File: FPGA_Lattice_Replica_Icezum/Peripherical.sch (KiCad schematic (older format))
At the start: 33 parts, among them J15 1x4_male_pin_Header_2.54mm, J16 1x4_male_pin_Header_2.54mm, J17 1x4_male_pin_Header_2.54mm, SW1 SW1, SW2 Switch_4p, U7 ADS7924

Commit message: se corrigieron errores de huellas y referencias que genereban errores cuando se hacia el diseño PCB
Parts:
- LD0, LD1, LD2, LD3, LD4, LD5, LD6, LD7: symbol Device:LED -> icezum:LED
- R17, R18: footprint footprints:R_Array_Convex_4x0603 -> footprints:R_0402
- SW1, SW2: symbol icezum:Switch_4p -> icezum:Switch
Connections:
- net +3V3: now also SW1.2, SW2.2; no longer SW1.3, SW1.4, SW2.3, SW2.4
- net GND: now also LD0.K, LD1.K, LD2.K, LD3.K, LD4.K, LD5.K, LD6.K, LD7.K; no longer LD0.1 (K), LD1.1 (K), LD2.1 (K), LD3.1 (K), LD4.1 (K), LD5.1 (K), LD6.1 (K), LD7.1 (K)
- net U_SW1: no longer SW1.2
- net U_SW2: no longer SW2.2
- net at R17.1: now also LD0.A; no longer LD0.2 (A)
- net at R18.1: now also LD1.A; no longer LD1.2 (A)
- net at R40.1: now also LD2.A; no longer LD2.2 (A)
- net at R41.1: now also LD3.A; no longer LD3.2 (A)
- net at R42.1: now also LD4.A; no longer LD4.2 (A)
- net at R43.1: now also LD5.A; no longer LD5.2 (A)
- net at R44.1: now also LD6.A; no longer LD6.2 (A)
- net at R45.1: now also LD7.A; no longer LD7.2 (A)
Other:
- moved on the sheet: SW1, SW2
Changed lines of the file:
@@
 $EndDescr
 $Comp
-L Device:LED LD0
+L icezum:LED LD0
 U 1 1 5D1D395A
-P 9200 1500
-F 0 "LD0" H 9193 1245 50  0000 C CNN
-F 1 "Green" H 9193 1336 50  0000 C CNN
-F 2 "footprints:LED_0603" H 9200 1500 50  0001 C CNN
-F 3 "~" H 9200 1500 50  0001 C CNN
-	1    9200 1500
-	-1   0    0    1
-$EndComp
-$Comp
-L Device:LED LD1
+P 8950 1500
+F 0 "LD0" H 9200 1300 50  0000 C CNN
+F 1 "Green" H 9050 1400 50  0000 C CNN
+F 2 "footprints:LED_0603" H 8950 1500 50  0001 C CNN
+F 3 "~" H 8950 1500 50  0001 C CNN
+	1    8950 1500
+	1    0    0    -1
+$EndComp
+$Comp
+L icezum:LED LD1
 U 1 1 5D1D4304
-P 9200 2000
-F 0 "LD1" H 9193 1745 50  0000 C CNN
-F 1 "Green" H 9193 1836 50  0000 C CNN
-F 2 "footprints:LED_0603" H 9200 2000 50  0001 C CNN
-F 3 "~" H 9200 2000 50  0001 C CNN
-	1    9200 2000
-	-1   0    0    1
-$EndComp
-$Comp
-L Device:LED LD2
+P 8950 2000
+F 0 "LD1" H 9200 1800 50  0000 C CNN
+F 1 "Green" H 9050 1900 50  0000 C CNN
+F 2 "footprints:LED_0603" H 8950 2000 50  0001 C CNN
+F 3 "~" H 8950 2000 50  0001 C CNN
+	1    8950 2000
+	1    0    0    -1
+$EndComp
+$Comp
+L icezum:LED LD2
 U 1 1 5D1D467C
-P 9200 2550
-F 0 "LD2" H 9193 2295 50  0000 C CNN
-F 1 "Green" H 9193 2386 50  0000 C CNN
-F 2 "footprints:LED_0603" H 9200 2550 50  0001 C CNN
-F 3 "~" H 9200 2550 50  0001 C CNN
-	1    9200 2550
-	-1   0    0    1
-$EndComp
-$Comp
-L Device:LED LD3
+P 8950 2550
+F 0 "LD2" H 9200 2350 50  0000 C CNN
+F 1 "Green" H 9050 2450 50  0000 C CNN
+F 2 "footprints:LED_0603" H 8950 2550 50  0001 C CNN
+F 3 "~" H 8950 2550 50  0001 C CNN
+	1    8950 2550
+	1    0    0    -1
+$EndComp
+$Comp
+L icezum:LED LD3
 U 1 1 5D1D4941
-P 9200 3100
-F 0 "LD3" H 9193 2845 50  0000 C CNN
-F 1 "Green" H 9193 2936 50  0000 C CNN
-F 2 "footprints:LED_0603" H 9200 3100 50  0001 C CNN
-F 3 "~" H 9200 3100 50  0001 C CNN
-	1    9200 3100
-	-1   0    0    1
-$EndComp
-$Comp
-L Device:LED LD4
+P 8950 3100
+F 0 "LD3" H 9200 2900 50  0000 C CNN
+F 1 "Green" H 9050 3000 50  0000 C CNN
+F 2 "footprints:LED_0603" H 8950 3100 50  0001 C CNN
+F 3 "~" H 8950 3100 50  0001 C CNN
+	1    8950 3100
+	1    0    0    -1
+$EndComp
+$Comp
+L icezum:LED LD4
 U 1 1 5D1D4BE4
-P 9200 3700
-F 0 "LD4" H 9193 3445 50  0000 C CNN
-F 1 "Green" H 9193 3536 50  0000 C CNN
-F 2 "footprints:LED_0603" H 9200 3700 50  0001 C CNN
-F 3 "~" H 9200 3700 50  0001 C CNN
-	1    9200 3700
-	-1   0    0    1
-$EndComp
-$Comp
-L Device:LED LD5
+P 8950 3700
+F 0 "LD4" H 9200 3500 50  0000 C CNN
+F 1 "Green" H 9050 3600 50  0000 C CNN
+F 2 "footprints:LED_0603" H 8950 3700 50  0001 C CNN
+F 3 "~" H 8950 3700 50  0001 C CNN
+	1    8950 3700
+	1    0    0    -1
+$EndComp
+$Comp
+L icezum:LED LD5
 U 1 1 5D1D4EB3
-P 9200 4300
-F 0 "LD5" H 9193 4045 50  0000 C CNN
-F 1 "Green" H 9193 4136 50  0000 C CNN
-F 2 "footprints:LED_0603" H 9200 4300 50  0001 C CNN
-F 3 "~" H 9200 4300 50  0001 C CNN
-	1    9200 4300
-	-1   0    0    1
-$EndComp
-$Comp
-L Device:LED LD6
+P 8950 4300
+F 0 "LD5" H 9200 4100 50  0000 C CNN
+F 1 "Green" H 9050 4200 50  0000 C CNN
+F 2 "footprints:LED_0603" H 8950 4300 50  0001 C CNN
+F 3 "~" H 8950 4300 50  0001 C CNN
+	1    8950 4300
+	1    0    0    -1
+$EndComp
+$Comp
+L icezum:LED LD6
 U 1 1 5D1D527D
-P 9200 4850
-F 0 "LD6" H 9193 4595 50  0000 C CNN
-F 1 "Green" H 9193 4686 50  0000 C CNN
-F 2 "footprints:LED_0603" H 9200 4850 50  0001 C CNN
-F 3 "~" H 9200 4850 50  0001 C CNN
-	1    9200 4850
-	-1   0    0    1
-$EndComp
-$Comp
-L Device:LED LD7
+P 8950 4850
+F 0 "LD6" H 9200 4650 50  0000 C CNN
+F 1 "Green" H 9050 4750 50  0000 C CNN
+F 2 "footprints:LED_0603" H 8950 4850 50  0001 C CNN
+F 3 "~" H 8950 4850 50  0001 C CNN
+	1    8950 4850
+	1    0    0    -1
+$EndComp
+$Comp
+L icezum:LED LD7
 U 1 1 5D1D55BB
-P 9200 5400
-F 0 "LD7" H 9193 5145 50  0000 C CNN
-F 1 "Green" H 9193 5236 50  0000 C CNN
-F 2 "footprints:LED_0603" H 9200 5400 50  0001 C CNN
-F 3 "~" H 9200 5400 50  0001 C CNN
-	1    9200 5400
-	-1   0    0    1
+P 8950 5400
+F 0 "LD7" H 9200 5200 50  0000 C CNN
+F 1 "Green" H 9050 5300 50  0000 C CNN
+F 2 "footprints:LED_0603" H 8950 5400 50  0001 C CNN
+F 3 "~" H 8950 5400 50  0001 C CNN
+	1    8950 5400
+	1    0    0    -1
 $EndComp
 $Comp
@@
 F 0 "R17" V 8393 1500 50  0000 C CNN
 F 1 "2K2±5% 0.063W" V 8484 1500 50  0000 C CNN
-F 2 "footprints:R_Array_Convex_4x0603" V 8530 1500 50  0001 C CNN
+F 2 "footprints:R_0402" V 8530 1500 50  0001 C CNN
 F 3 "~" H 8600 1500 50  0001 C CNN
 	1    8600 1500
@@
 F 0 "R18" V 8393 2000 50  0000 C CNN
 F 1 "2K2±5% 0.063W" V 8484 2000 50  0000 C CNN
-F 2 "footprints:R_Array_Convex_4x0603" V 8530 2000 50  0001 C CNN
+F 2 "footprints:R_0402" V 8530 2000 50  0001 C CNN
 F 3 "~" H 8600 2000 50  0001 C CNN
 	1    8600 2000
@@
 	1    0    0    -1
 $EndComp
-Wire Wire Line
-	9350 1500 9650 1500
-Wire Wire Line
-	9650 1500 9650 2000
-Wire Wire Line
-	9350 5400 9650 5400
-Connection ~ 9650 5400
-Wire Wire Line
-	9650 5400 9650 5700
-Wire Wire Line
-	9350 4850 9650 4850
-Connection ~ 9650 4850
-Wire Wire Line
-	9650 4850 9650 5400
-Wire Wire Line
-	9350 4300 9650 4300
-Connection ~ 9650 4300
-Wire Wire Line
-	9650 4300 9650 4850
-Wire Wire Line
-	9350 3700 9650 3700
-Connection ~ 9650 3700
-Wire Wire Line
-	9650 3700 9650 4300
-Wire Wire Line
-	9350 3100 9650 3100
-Connection ~ 9650 3100
-Wire Wire Line
-	9650 3100 9650 3700
-Wire Wire Line
-	9350 2550 9650 2550
-Connection ~ 9650 2550
-Wire Wire Line
-	9650 2550 9650 3100
-Wire Wire Line
-	9350 2000 9650 2000
-Connection ~ 9650 2000
-Wire Wire Line
-	9650 2000 9650 2550
-Wire Wire Line
-	8750 1500 9050 1500
-Wire Wire Line
-	8750 2000 9050 2000
-Wire Wire Line
-	8750 2550 9050 2550
-Wire Wire Line
-	8750 3100 9050 3100
-Wire Wire Line
-	8750 3700 9050 3700
-Wire Wire Line
-	8750 4300 9050 4300
-Wire Wire Line
-	8750 4850 9050 4850
-Wire Wire Line
-	8750 5400 9050 5400
 Text GLabel 8000 1500 0    50   Input ~ 0
 LED_0
@@
 	1850 800  1850 1000
 $Comp
-L icezum:Switch_4p SW1
+L icezum:Switch SW1
 U 1 1 5D2428C1
 P 4200 5550
@@
 $EndComp
 $Comp
-L icezum:Switch_4p SW2
+L icezum:Switch SW2
 U 1 1 5D243575
 P 4250 6650
@@
 	3650 7100 3650 6950
 Wire Wire Line
-	4250 6650 4250 6750
-Wire Wire Line
 	4250 6650 3650 6650
-Connection ~ 4250 6650
 Wire Wire Line
 	3650 6650 3150 6650
 Connection ~ 3650 6650
 Wire Wire Line
-	4200 5650 4200 5550
-Wire Wire Line
 	4200 5550 3650 5550
-Connection ~ 4200 5550
 Wire Wire Line
 	3650 5550 3150 5550
 Connection ~ 3650 5550
 Wire Wire Line
-	5000 6750 5000 6650
-Wire Wire Line
 	5000 6650 5500 6650
 Wire Wire Line
 	5500 6650 5500 6550
-Connection ~ 5000 6650
-Wire Wire Line
-	4950 5650 4950 5550
 Wire Wire Line
 	4950 5550 5550 5550
 Wire Wire Line
 	5550 5550 5550 5450
-Connection ~ 4950 5550
 Text GLabel 2800 5550 0    50   Output ~ 0
 U_SW1
@@
 Text Notes 3000 4850 0    129  ~ 26
 Switch buttons 1 and 2
+Wire Wire Line
+	9500 1500 9650 1500
+Wire Wire Line
+	9500 2000 9650 2000
+Wire Wire Line
+	9650 1500 9650 2000
+Connection ~ 9650 2000
+Wire Wire Line
+	9650 2000 9650 2550
+Wire Wire Line
+	9500 2550 9650 2550
+Connection ~ 9650 2550
+Wire Wire Line
+	9650 2550 9650 3100
+Wire Wire Line
+	9500 3100 9650 3100
+Connection ~ 9650 3100
+Wire Wire Line
+	9650 3100 9650 3700
+Wire Wire Line
+	9500 3700 9650 3700
+Connection ~ 9650 3700
+Wire Wire Line
+	9650 3700 9650 4300
+Wire Wire Line
+	9500 4300 9650 4300
+Connection ~ 9650 4300
+Wire Wire Line
+	9650 4300 9650 4850
+Wire Wire Line
+	9500 4850 9650 4850
+Connection ~ 9650 4850
+Wire Wire Line
+	8750 1500 8950 1500
+Wire Wire Line
+	8750 2000 8950 2000
+Wire Wire Line
+	8750 2550 8950 2550
+Wire Wire Line
+	8750 3100 8950 3100
+Wire Wire Line
+	8750 3700 8950 3700
+Wire Wire Line
+	8750 4300 8950 4300
+Wire Wire Line
+	8750 4850 8950 4850
+Wire Wire Line
+	9650 4850 9650 5400
+Wire Wire Line
+	8750 5400 8950 5400
+Wire Wire Line
+	9500 5400 9650 5400
+Connection ~ 9650 5400
+Wire Wire Line
+	9650 5400 9650 5700
 $EndSCHEMATC

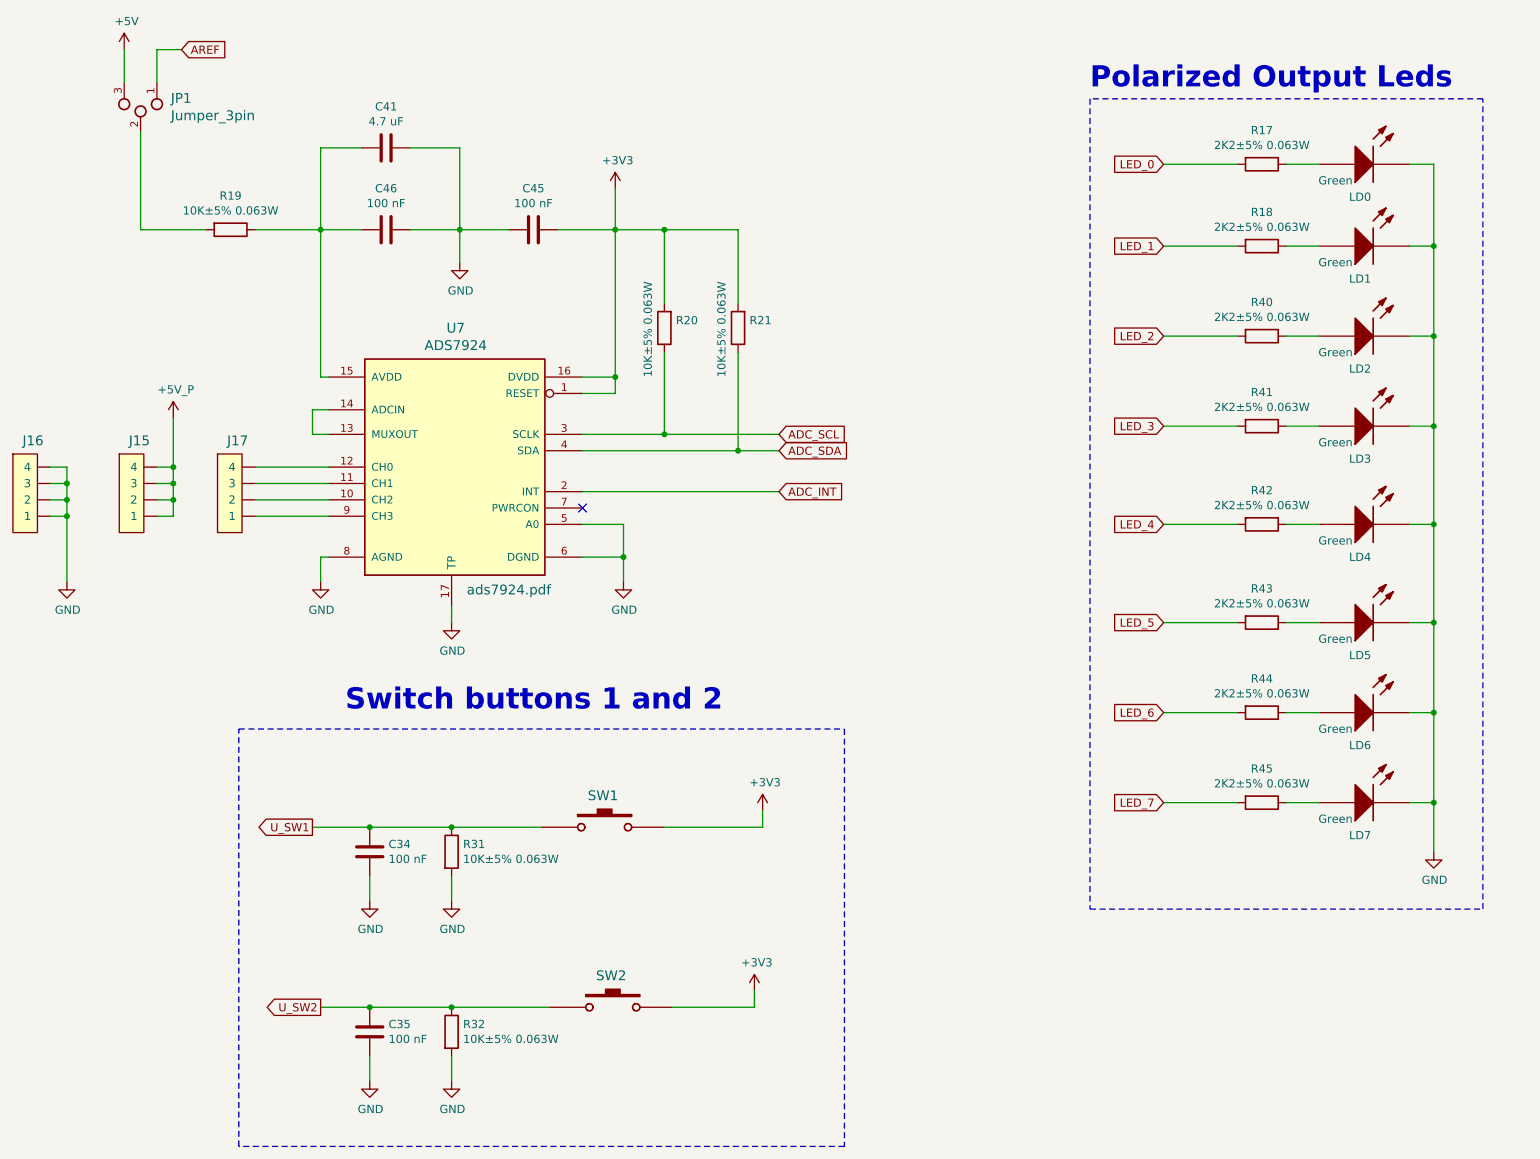
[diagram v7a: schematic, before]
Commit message: se mejoro esquematico de acuerdo a la revisión del docente. Se mejoro rotulo (se coloco link del repo, autor y autor de la versión original y la licencia) se mejoro el flujo izquiera derecha de los botones, se desplazo fiduciales a la página principal, se achico el esquematico en la parte de headers
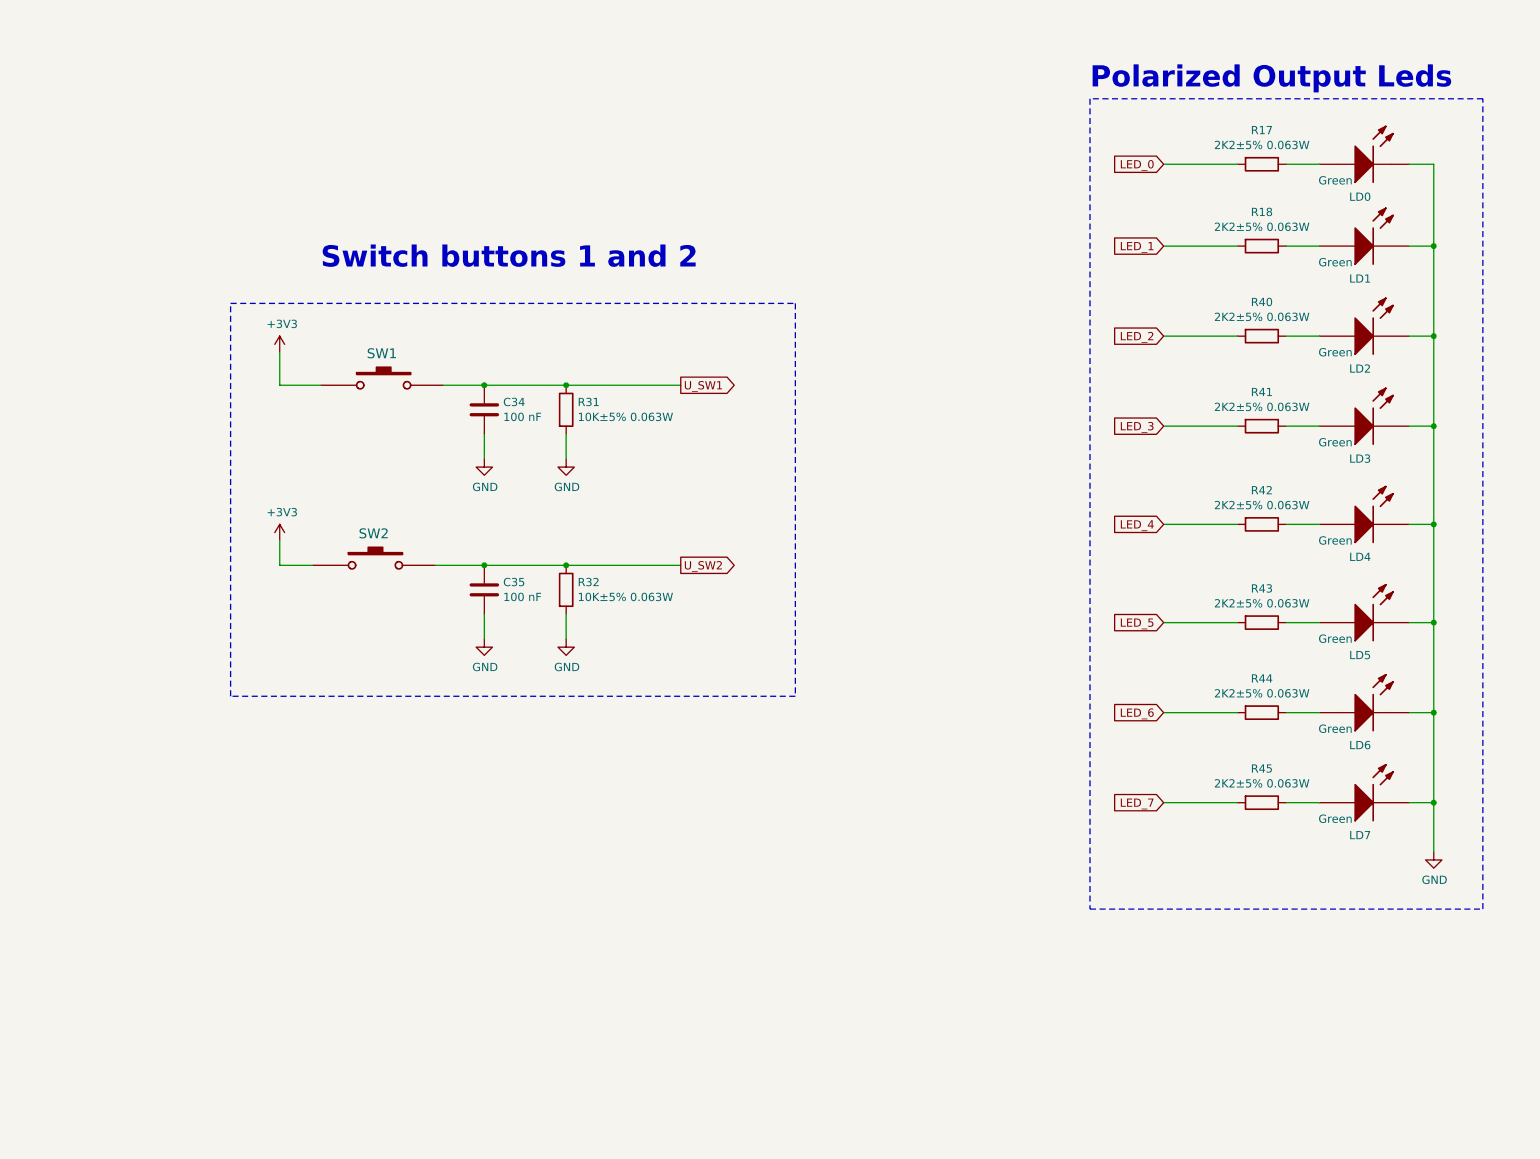
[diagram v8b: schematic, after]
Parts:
- removed C41: 4.7 uF, footprints:C_0603, symbol Device:C
- removed C45, C46: 100 nF, footprints:C_0402, symbol Device:C
- removed J15, J16, J17: 1x4_male_pin_Header_2.54mm, footprints:1x04-pin-header-2.54mm, symbol icezum:1x4_male_pin_Header_2.54mm
- removed JP1: Jumper_3pin, footprints:1x03-pin-header-2.54mm, symbol icezum:Jumper_3pin
- removed R19, R20, R21: 10K±5% 0.063W, footprints:R_0402, symbol Device:R
- removed U7: ADS7924, footprints:QFN16, symbol icezum:ADS7924
- C34, C35: footprint footprints:C_0402 -> footprints:L_0805
- R17, R18, R31, R32, R40, R41, R42, R43, R44, R45: footprint footprints:R_0402 -> footprints:F_0805
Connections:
- net +3V3: now also SW1.1, SW2.1; no longer SW1.2, SW2.2
- net U_SW1: now also SW1.2; no longer SW1.1
- net U_SW2: now also SW2.2; no longer SW2.1
- no-connect marks 1 -> 0
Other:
- moved on the sheet: C34, C35, R31, R32, SW1, SW2
